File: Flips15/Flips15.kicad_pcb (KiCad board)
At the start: 2 copper layers, 100 x 100 mm, 68 parts, among them CN1 UFP2810, U1001 74HC238, U1002 ULN2803A, U1003 74HC238, U1004 TBD62783A, U1101 74HC238, U1102 ULN2803A, U1103 74HC238, U1104 TBD62783A, U701 74HC238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

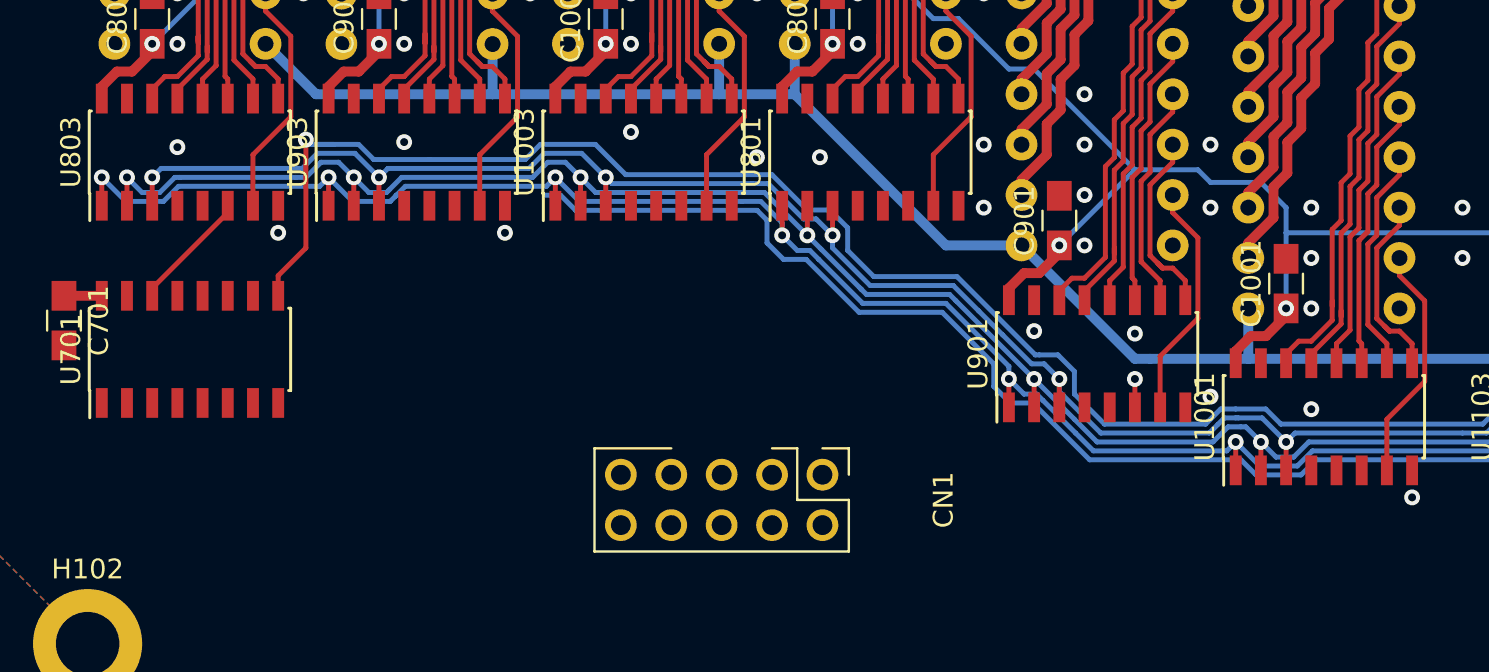
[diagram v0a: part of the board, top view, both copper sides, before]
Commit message: connecting enable lines of 8 decoders
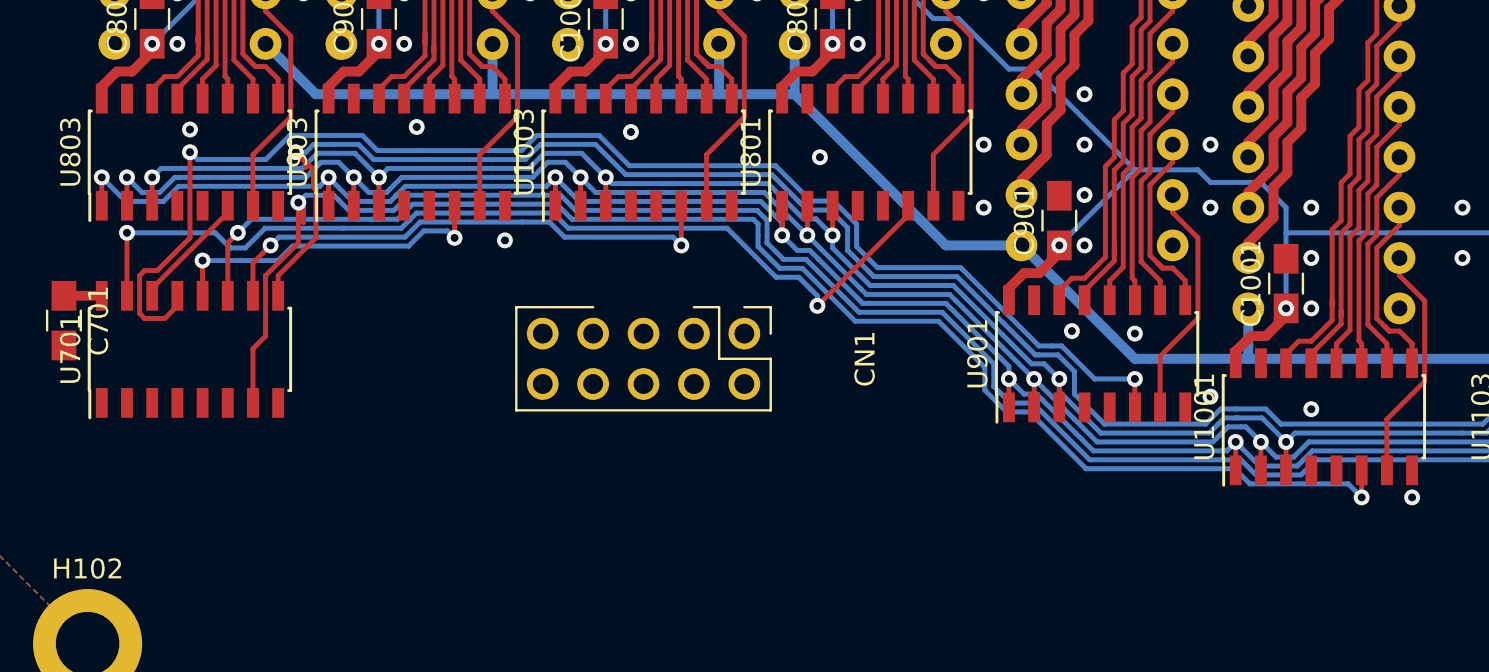
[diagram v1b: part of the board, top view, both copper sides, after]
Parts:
- moved CN1 8.13 mm to (88.9, 130.2)
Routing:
- net /UnitY/E2L: track 0.00 -> 70.5 mm, vias 0 -> 2
- net /UnitY/E1L: track 1.43 -> 68.4 mm, vias 1 -> 2
- net /UnitY/E0L: track 0.00 -> 48.2 mm, vias 0 -> 2
- net /UnitY/E2H: track 0.00 -> 26.6 mm, vias 0 -> 2
- net /UnitY/E3H: track 64.8 -> 90.2 mm, vias 1 -> 2
- net /UnitY/E1H: track 0.00 -> 16.9 mm, vias 0 -> 2
- net GND: vias 85 -> 83

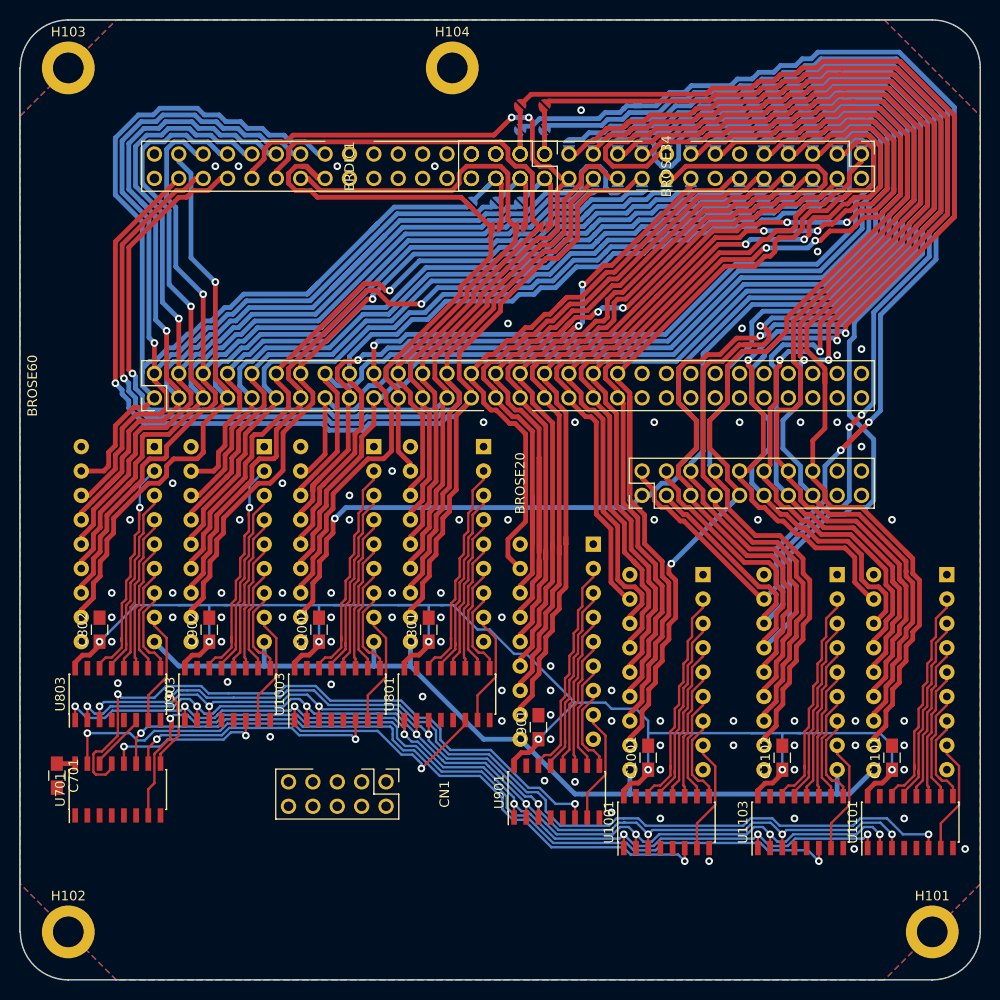
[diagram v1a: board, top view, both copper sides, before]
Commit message: moving pcb to get space for upper right mounting hole
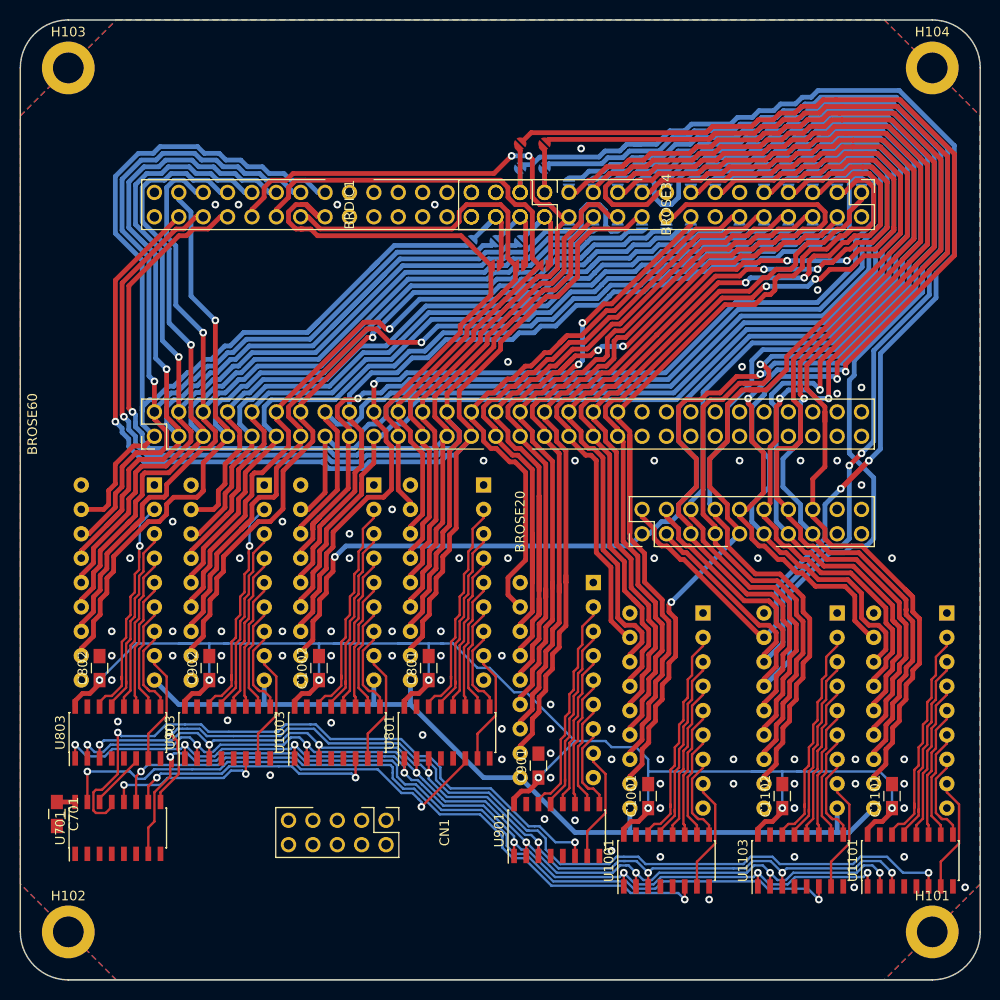
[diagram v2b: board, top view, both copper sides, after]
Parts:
- moved H104 50.0 mm to (145.8, 55.8)
- moved JP115 4.00 mm to (128.3, 67.8)
- moved JP116 4.00 mm to (130.8, 67.8)
- moved JP117 4.00 mm to (133.3, 67.8)
- moved JP118 4.00 mm to (138.4, 67.8)
- moved JP119 4.00 mm to (123.2, 67.8)
- moved JP120 4.00 mm to (135.9, 67.8)
- moved JP121 4.00 mm to (120.7, 67.8)
- moved JP122 4.00 mm to (102.9, 66.2)
- moved JP123 4.00 mm to (105.4, 66.2)
- moved JP124 4.00 mm to (108.0, 67.8)
- moved JP125 4.00 mm to (110.5, 67.8)
- moved JP126 4.00 mm to (115.6, 67.8)
- moved JP127 4.00 mm to (113.0, 67.8)
- moved JP128 4.00 mm to (118.1, 67.8)
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
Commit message: Finish remaining connection on Flips15
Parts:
- moved CN1 2.98 mm to (88.9, 137.2)
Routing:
- net /UnitY/DATA: track 0.00 -> 48.0 mm
- net VCC: track 162.0 -> 208.3 mm, vias 8 -> 9
- net /UnitY/B1: track 0.00 -> 37.3 mm
- net /UnitY/B0: track 0.00 -> 36.4 mm
- net /UnitY/EN: track 0.00 -> 30.6 mm
- net +24V: track 95.3 -> 118.1 mm
- net /UnitY/A2: track 105.0 -> 123.7 mm
- net /UnitY/A1: track 105.5 -> 118.4 mm
- net /UnitY/A0: track 104.8 -> 114.5 mm
- net /UnitY/Group2/YL7: track 12.0 -> 13.1 mm
- net /UnitY/Group0/YL6: track 9.71 -> 10.4 mm
- net /UnitY/Group0/YL7: track 12.0 -> 12.5 mm
- net /UnitY/Group3/YL7: track 12.0 -> 12.5 mm
- net /UnitY/Group1/YL7: track 12.0 -> 12.5 mm
- net GND: vias 83 -> 81

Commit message: improve traces
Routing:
- net /UnitY/E3L: track 100.2 -> 98.2 mm
- net /UnitY/A2: track 123.7 -> 122.3 mm
- net /UnitY/E2L: track 70.5 -> 69.2 mm
- net /UnitY/E3H: track 90.2 -> 88.8 mm
- net /UnitY/A0: track 114.5 -> 113.4 mm
- net /UnitY/E1L: track 68.4 -> 67.8 mm

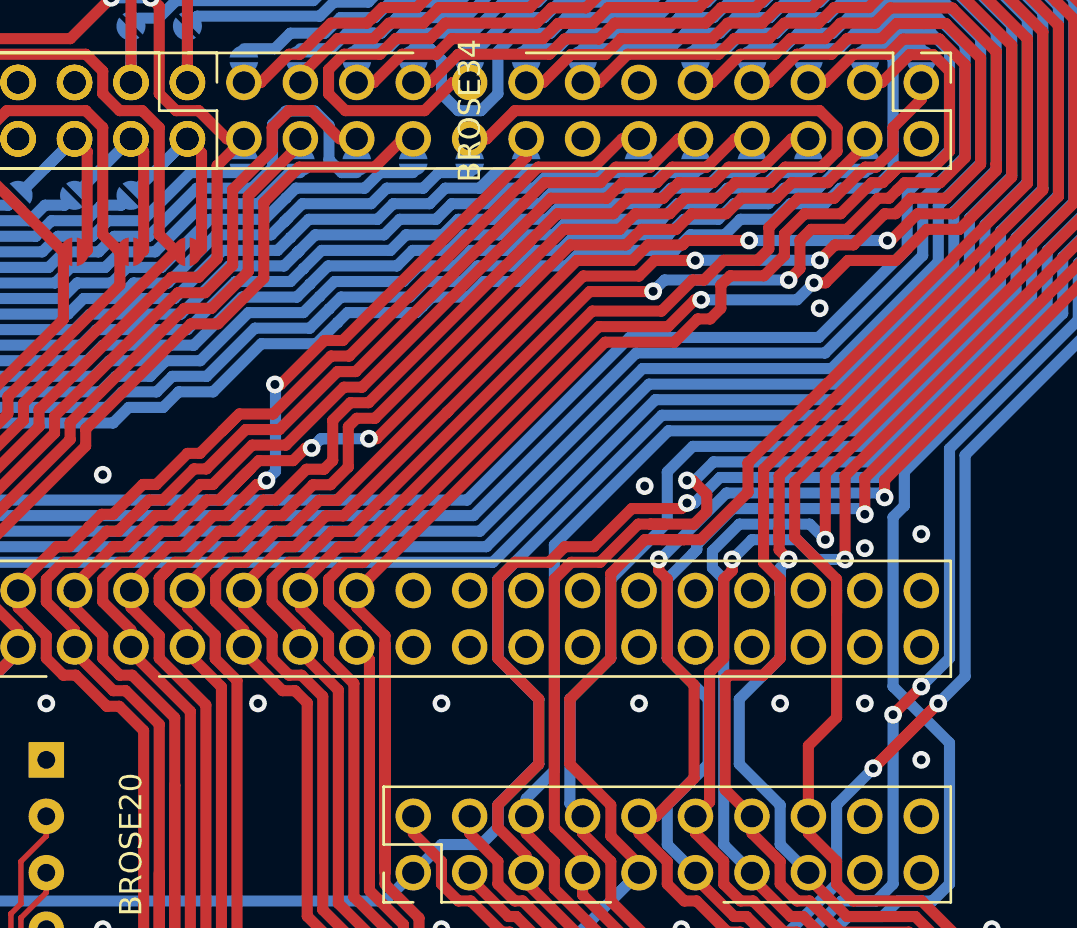
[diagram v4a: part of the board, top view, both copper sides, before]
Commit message: minor changes in traces
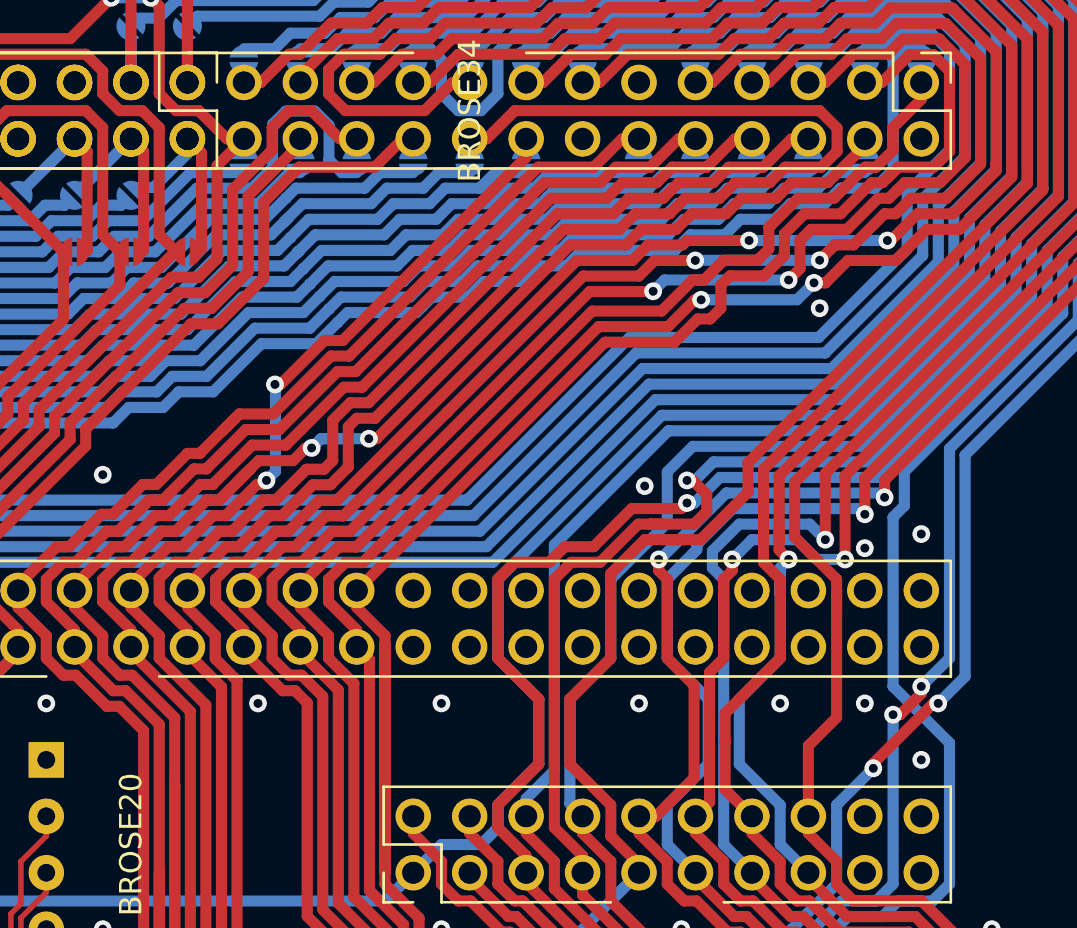
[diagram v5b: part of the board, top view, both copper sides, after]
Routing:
- net /SY22: track 133.7 -> 130.0 mm
- net /T2: track 10.3 -> 8.87 mm
- net /X26: track 107.6 -> 106.7 mm
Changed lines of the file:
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@@
     (thickness 1.6)
     (drawings 8)
-    (tracks 3841)
+    (tracks 3845)
     (zones 0)
     (modules 68)
@@
   (segment (start 130.81 102.552) (end 132.08 103.822) (width 0.5) (layer F.Cu) (net 16) (status 400010))
   (segment (start 132.08 91.122) (end 132.08 94.678) (width 0.5) (layer F.Cu) (net 16))
-  (segment (start 132.08 94.678) (end 131.318 95.44) (width 0.5) (layer F.Cu) (net 16))
+  (segment (start 132.08 94.678) (end 131.54 95.218) (width 0.5) (layer F.Cu) (net 16))
   (segment (start 123.929074 66.813022) (end 124.6421 66.099996) (width 0.5) (layer F.Cu) (net 16))
   (segment (start 128.732148 66.099996) (end 129.43215 65.399994) (width 0.5) (layer F.Cu) (net 16))
@@
   (segment (start 132.08 91.122) (end 131.333483 90.375483) (width 0.5) (layer F.Cu) (net 16))
   (segment (start 130.81 101.79) (end 129.605002 100.585002) (width 0.5) (layer F.Cu) (net 16) (status 400010))
-  (segment (start 129.605002 100.585002) (end 129.605002 95.60295) (width 0.5) (layer F.Cu) (net 16))
-  (segment (start 129.767952 95.44) (end 129.605002 95.60295) (width 0.5) (layer F.Cu) (net 16))
-  (segment (start 131.318 95.44) (end 129.767952 95.44) (width 0.5) (layer F.Cu) (net 16))
+  (segment (start 129.605002 100.585002) (end 129.605002 98.425) (width 0.5) (layer F.Cu) (net 16))
+  (segment (start 131.54 95.218) (end 129.605002 97.152998) (width 0.5) (layer F.Cu) (net 16))
+  (segment (start 129.605002 97.152998) (end 129.605002 98.425) (width 0.5) (layer F.Cu) (net 16))
   (segment (start 97.79 94.17) (end 97.79 94.397952) (width 0.5) (layer F.Cu) (net 17) (status C00030))
   (segment (start 96.21001 103.74775) (end 96.21001 95.977942) (width 0.5) (layer F.Cu) (net 17))
@@
   (segment (start 115.57 102.552) (end 116.84 103.822) (width 0.5) (layer F.Cu) (net 45) (status 400010))
   (segment (start 119.917052 107.000004) (end 119.5621 107.000004) (width 0.5) (layer F.Cu) (net 45))
-  (segment (start 139.192 96.71) (end 136.271 99.631) (width 0.5) (layer F.Cu) (net 45))
   (via (at 139.192 96.71) (size 0.8) (drill 0.4) (layers F.Cu B.Cu) (net 45))
   (segment (start 140.400002 95.501998) (end 139.192 96.71) (width 0.5) (layer B.Cu) (net 45))
@@
   (segment (start 134.62 104.838) (end 129.54 109.918) (width 0.5) (layer B.Cu) (net 45))
   (segment (start 129.54 113.855) (end 128.27 115.125) (width 0.5) (layer B.Cu) (net 45) (status 800020))
-  (segment (start 138.938 96.964) (end 136.271 99.631) (width 0.5) (layer F.Cu) (net 45))
   (segment (start 113.2602 64.452992) (end 113.653596 64.059596) (width 0.5) (layer B.Cu) (net 45))
   (segment (start 113.653596 64.059596) (end 113.717096 63.996096) (width 0.5) (layer B.Cu) (net 45))
@@
   (segment (start 114.808 63.75299) (end 117.060298 63.75299) (width 0.5) (layer B.Cu) (net 45))
   (segment (start 114.808 63.75299) (end 115.443 63.75299) (width 0.5) (layer B.Cu) (net 45))
+  (segment (start 139.192 96.71) (end 138.975952 96.71) (width 0.5) (layer F.Cu) (net 45))
+  (segment (start 136.271 99.414952) (end 136.271 99.631) (width 0.5) (layer F.Cu) (net 45))
+  (segment (start 138.975952 96.71) (end 136.271 99.414952) (width 0.5) (layer F.Cu) (net 45))
   (segment (start 118.11 104.33) (end 118.11 104.557952) (width 0.5) (layer F.Cu) (net 46) (status C00030))
   (segment (start 118.11 104.557952) (end 119.85205 106.300002) (width 0.5) (layer F.Cu) (net 46) (status 10))
@@
   (via (at 138.43 95.948) (size 0.8) (drill 0.4) (layers F.Cu B.Cu) (net 46))
   (via (at 137.16 97.218) (size 0.8) (drill 0.4) (layers F.Cu B.Cu) (net 46))
-  (segment (start 139.7 85.247472) (end 139.7 94.678) (width 0.5) (layer B.Cu) (net 46))
-  (segment (start 134.847952 105.6) (end 130.240002 110.20795) (width 0.5) (layer B.Cu) (net 46))
-  (segment (start 136.398 105.6) (end 134.847952 105.6) (width 0.5) (layer B.Cu) (net 46))
-  (segment (start 137.16 104.838) (end 136.398 105.6) (width 0.5) (layer B.Cu) (net 46))
-  (segment (start 137.16 97.218) (end 137.16 104.838) (width 0.5) (layer B.Cu) (net 46))
+  (segment (start 130.240002 115.694998) (end 128.27 117.665) (width 0.5) (layer B.Cu) (net 46) (status 800020))
   (segment (start 130.240002 110.20795) (end 130.240002 115.694998) (width 0.5) (layer B.Cu) (net 46))
+  (segment (start 137.16 97.218) (end 137.16 104.838) (width 0.5) (layer B.Cu) (net 46))
+  (segment (start 137.16 104.838) (end 136.398 105.6) (width 0.5) (layer B.Cu) (net 46))
+  (segment (start 136.398 105.6) (end 134.847952 105.6) (width 0.5) (layer B.Cu) (net 46))
+  (segment (start 134.847952 105.6) (end 130.240002 110.20795) (width 0.5) (layer B.Cu) (net 46))
+  (segment (start 139.7 85.247472) (end 139.7 94.678) (width 0.5) (layer B.Cu) (net 46))
   (segment (start 147.400022 75.00745) (end 145.495022 76.91245) (width 0.5) (layer B.Cu) (net 46))
   (segment (start 145.495022 76.91245) (end 145.495022 79.45245) (width 0.5) (layer B.Cu) (net 46))
@@
   (segment (start 132.540502 59.552978) (end 133.481598 59.552978) (width 0.5) (layer B.Cu) (net 46))
   (segment (start 133.481598 59.552978) (end 134.1816 58.852976) (width 0.5) (layer B.Cu) (net 46))
-  (segment (start 130.240002 115.694998) (end 128.27 117.665) (width 0.5) (layer B.Cu) (net 46) (status 800020))
   (segment (start 147.400022 64.18355) (end 142.069448 58.852976) (width 0.5) (layer B.Cu) (net 46))
   (segment (start 142.069448 58.852976) (end 134.1816 58.852976) (width 0.5) (layer B.Cu) (net 46))
@@
   (segment (start 120.3003 63.052988) (end 118.750252 63.052988) (width 0.5) (layer B.Cu) (net 46))
   (segment (start 121.000302 62.352986) (end 120.3003 63.052988) (width 0.5) (layer B.Cu) (net 46))
-  (segment (start 138.43 95.948) (end 137.16 97.218) (width 0.5) (layer F.Cu) (net 46))
   (segment (start 117.350248 64.452992) (end 114.250152 64.452992) (width 0.5) (layer B.Cu) (net 46))
   (segment (start 114.250152 64.452992) (end 113.55015 65.152994) (width 0.5) (layer B.Cu) (net 46))
@@
   (segment (start 105.76426 65.87574) (end 105.852998 65.787002) (width 0.5) (layer B.Cu) (net 46) (status C00030))
   (segment (start 105.852998 65.787002) (end 111.366094 65.787002) (width 0.5) (layer B.Cu) (net 46) (status 400010))
+  (segment (start 138.43 95.948) (end 138.43 96.266) (width 0.5) (layer F.Cu) (net 46))
+  (segment (start 137.478 97.218) (end 137.16 97.218) (width 0.5) (layer F.Cu) (net 46))
+  (segment (start 138.43 96.266) (end 137.478 97.218) (width 0.5) (layer F.Cu) (net 46))
   (segment (start 119.38 104.838) (end 120.142 105.6) (width 0.5) (layer F.Cu) (net 47))
   (segment (start 130.240002 114.32705) (end 129.54 113.627048) (width 0.5) (layer F.Cu) (net 47))
@@
   (segment (start 105.41 68.77) (end 105.41 64.402396) (width 0.5) (layer F.Cu) (net 176) (status 400010))
   (segment (start 105.41 64.402396) (end 105.053802 64.046198) (width 0.5) (layer F.Cu) (net 176) (status 800020))
-  (segment (start 104.14 72.58) (end 105.41 71.31) (width 0.5) (layer B.Cu) (net 177) (status 800020))
-  (segment (start 105.41 71.31) (end 103.226198 73.493802) (width 0.5) (layer B.Cu) (net 177) (status C00030))
   (segment (start 105.91374 76.39) (end 106.045 76.25874) (width 0.5) (layer F.Cu) (net 177) (status C00030))
   (segment (start 106.045 71.945) (end 105.41 71.31) (width 0.5) (layer F.Cu) (net 177) (status C00030))
   (segment (start 106.045 76.25874) (end 106.045 71.945) (width 0.5) (layer F.Cu) (net 177) (status C00030))
+  (segment (start 103.226198 73.493802) (end 103.887246 73.493802) (width 0.5) (layer B.Cu) (net 177) (status 400000))
+  (segment (start 105.41 71.971048) (end 105.41 71.31) (width 0.5) (layer B.Cu) (net 177) (status C00000))
+  (segment (start 103.887246 73.493802) (end 105.41 71.971048) (width 0.5) (layer B.Cu) (net 177) (status 800000))
   (segment (start 102.87 67.881) (end 102.87 68.77) (width 0.5) (layer B.Cu) (net 178) (status 800020))
   (segment (start 102.87 68.77) (end 102.87 66.73374) (width 0.5) (layer B.Cu) (net 178) (status C00030))
